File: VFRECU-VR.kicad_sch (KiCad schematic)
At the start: 39 parts, among them J1 USB_B_Mini, J1 USB_C_Receptacle_USB2.0, J17 Conn_01x06, J4 1-776087-1, J7 MUSBD111M0, M1 Module-power_12and5V-0.2, M3 Module-knock-0.2, M5 Module-wbo-0.5, M6 Module:mega-mcu100/0.2, M7 Module-wbo-0.5, P1 Pad, P2 Pad, P3 Pad, P4 Pad, U4 JDY-33

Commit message: Don't need proofreading I'm a FREAK
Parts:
- removed R17: 56k, hellen-one-common:R0603, symbol hellen-one-common:Res
- removed R19: 12k, hellen-one-common:R0603, symbol hellen-one-common:Res
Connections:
- net IN_BUTTON2 renamed Clutch/kickstandswitch
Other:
- note removed: "Cam/Crank- offset"

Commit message: More routing changes
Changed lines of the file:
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@@
 	)
 	(junction
-		(at 312.42 33.02)
-		(diameter 0)
-		(color 0 0 0 0)
-	)
-	(junction
 		(at 346.71 166.37)
 		(diameter 0)
@@
 	)
 	(junction
+		(at 312.42 26.67)
+		(diameter 0)
+		(color 0 0 0 0)
+	)
+	(junction
 		(at 168.91 148.59)
 		(diameter 0)
@@
 	(bus
 		(pts
-			(xy 138.43 25.4) (xy 342.9 25.4)
+			(xy 138.43 26.67) (xy 312.42 26.67)
 		)
 		(stroke
@@
 	(bus
 		(pts
-			(xy 311.15 -27.94) (xy 311.15 33.02)
+			(xy 312.42 -27.94) (xy 312.42 26.67)
 		)
 		(stroke
@@
 		)
 	)
-	(bus
-		(pts
-			(xy 342.9 33.02) (xy 312.42 33.02)
-		)
-		(stroke
-			(width 0)
-			(type default)
-		)
-	)
 	(wire
 		(pts
@@
 	(bus
 		(pts
-			(xy 342.9 25.4) (xy 342.9 33.02)
+			(xy 312.42 26.67) (xy 312.42 54.61)
 		)
 		(stroke
@@
 	(bus
 		(pts
-			(xy 138.43 34.29) (xy 138.43 25.4)
+			(xy 138.43 34.29) (xy 138.43 26.67)
 		)
 		(stroke
@@
 		)
 	)
-	(bus
-		(pts
-			(xy 312.42 33.02) (xy 312.42 54.61)
-		)
-		(stroke
-			(width 0)
-			(type default)
-		)
-	)
 	(wire
 		(pts
@@
 	(bus
 		(pts
-			(xy 270.51 -27.94) (xy 311.15 -27.94)
+			(xy 270.51 -27.94) (xy 312.42 -27.94)
 		)
 		(stroke
@@
 		)
 		(stroke
-			(width 0)
-			(type default)
-		)
-	)
-	(bus
-		(pts
-			(xy 311.15 33.02) (xy 312.42 33.02)
-		)
-		(stroke

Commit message: Moved Ground Planes to Internal Layers
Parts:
- removed H2: MountingHole_Pad, MountingHole:MountingHole_3.2mm_M3_DIN965_Pad, symbol Mechanical:MountingHole_Pad
- removed J1: USB_C_Receptacle_USB2.0, Connector_USB:USB_C_Receptacle_XKB_U262-16XN-4BVC11, symbol Connector:USB_C_Receptacle_USB2.0
- removed J17 (x2): Conn_01x06, Connector_PinHeader_2.54mm:PinHeader_1x06_P2.54mm_Vertical, symbol Connector_Generic:Conn_01x06
- removed J7: MUSBD111M0, usbb:CONN4_BD111M0_AMP, symbol usbb:MUSBD111M0
- removed P1, P2, P3, P4: Pad, hellen-one-common:PAD-TH, symbol hellen-one-common:Pad
- removed R3, R6: 5.6k, hellen-one-common:R0603, symbol hellen-one-common:Res
- removed R30: 0, hellen-one-common:R0603, symbol hellen-one-common:Res
- removed R4: Jumper-Pad-Pad, hellen-one-common:PAD-0805-PAD, symbol hellen-one-common:Jumper-Pad-Pad
- added R4: 0, Resistor_SMD:R_0402_1005Metric, symbol Device:R
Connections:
- net INTAKEFLAP: now also J4.4; no longer J4.5
- net IN_AUX1: now also J4.12; no longer J4.13
- net IN_AUX2: now also J4.13; no longer J4.11
- net IN_FLEX: now also J4.11; no longer J4.12
- net OUT_LS2: now also J4.5; no longer J4.6
- net OUT_LS3: now also J4.6; no longer J4.4
- net PG_5VP: now also M6.N12 (SPI3_MOSI_(PC12)), R4.2
- net at M1.E6 (PG_5VP): now also R4.1
- net DC1_DIR: no longer names the net of M6.E21 (OUT_PWM4_(PC8))
- net DC1_PWM: no longer names the net of M6.E20 (OUT_PWM3_(PC7))
- net DC2_PWM: no longer names the net of M6.E22 (OUT_PWM5_(PC9))
- net VR1_THRESHOLD: no longer names the net of M6.E23 (OUT_PWM6_(PD14))
- no-connect marks 35 -> 31
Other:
- note removed: "A"

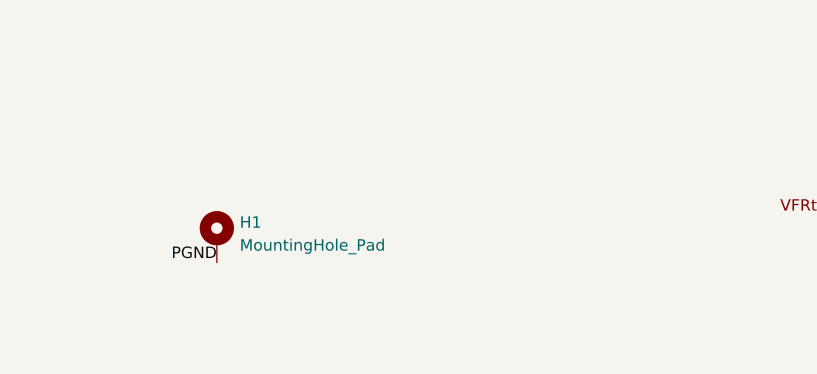
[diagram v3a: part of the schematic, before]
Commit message: Fixed pads
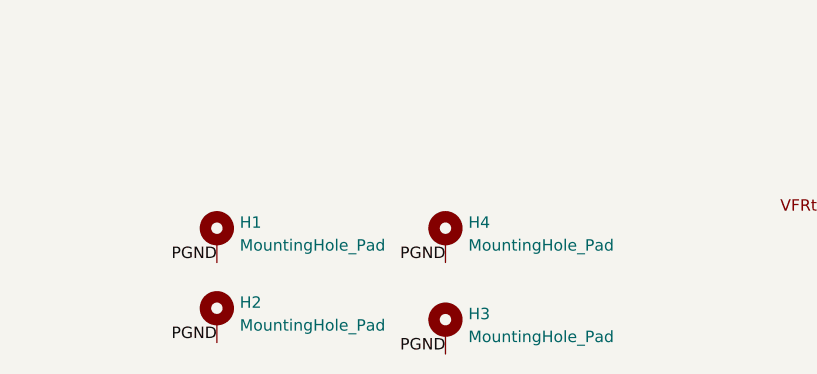
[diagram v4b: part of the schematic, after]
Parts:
- added H2, H3, H4: MountingHole_Pad, MountingHole:MountingHole_3.2mm_M3_DIN965_Pad, symbol Mechanical:MountingHole_Pad
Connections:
- net GND: now also H2.1, H3.1, H4.1
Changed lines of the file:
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@@
 		)
 	)
+	(label "PGND"
+		(at 228.6 401.32 180)
+		(fields_autoplaced yes)
+		(effects
+			(font
+				(size 1.27 1.27)
+			)
+			(justify right bottom)
+		)
+	)
 	(label "INJ3"
 		(at 247.65 138.43 0)
@@
 		)
 	)
+	(label "PGND"
+		(at 203.2 400.05 180)
+		(fields_autoplaced yes)
+		(effects
+			(font
+				(size 1.27 1.27)
+			)
+			(justify right bottom)
+		)
+	)
 	(label "VR1-"
 		(at 133.35 229.87 0)
@@
 		)
 	)
+	(label "PGND"
+		(at 228.6 391.16 180)
+		(fields_autoplaced yes)
+		(effects
+			(font
+				(size 1.27 1.27)
+			)
+			(justify right bottom)
+		)
+	)
 	(label "12VSWITCHED"
 		(at 138.43 148.59 90)
@@
 	(symbol
 		(lib_id "Mechanical:MountingHole_Pad")
+		(at 203.2 397.51 0)
+		(unit 1)
+		(exclude_from_sim no)
+		(in_bom yes)
+		(on_board yes)
+		(dnp no)
+		(fields_autoplaced yes)
+		(property "Reference" "H2"
+			(at 205.74 395.605 0)
+			(effects
+				(font
+					(size 1.27 1.27)
+				)
+				(justify left)
+			)
+		)
+		(property "Value" "MountingHole_Pad"
+			(at 205.74 398.145 0)
+			(effects
+				(font
+					(size 1.27 1.27)
+				)
+				(justify left)
+			)
+		)
+		(property "Footprint" "MountingHole:MountingHole_3.2mm_M3_DIN965_Pad"
+			(at 203.2 397.51 0)
+			(effects
+				(font
+					(size 1.27 1.27)
+				)
+				(hide yes)
+			)
+		)
+		(property "Datasheet" "~"
+			(at 203.2 397.51 0)
+			(effects
+				(font
+					(size 1.27 1.27)
+				)
+				(hide yes)
+			)
+		)
+		(property "Description" ""
+			(at 203.2 397.51 0)
+			(effects
+				(font
+					(size 1.27 1.27)
+				)
+				(hide yes)
+			)
+		)
+		(pin "1"
+		)
+		(instances
+			(project "VFRECU-VR"
+				(path "/90b72e19-92bc-40db-bd4d-f17fb5de93ea"
+					(reference "H2")
+					(unit 1)
+				)
+			)
+		)
+	)
+	(symbol
+		(lib_id "Mechanical:MountingHole_Pad")
 		(at 203.2 388.62 0)
 		(unit 1)
@@
 	)
 	(symbol
+		(lib_id "Mechanical:MountingHole_Pad")
+		(at 228.6 398.78 0)
+		(unit 1)
+		(exclude_from_sim no)
+		(in_bom yes)
+		(on_board yes)
+		(dnp no)
+		(fields_autoplaced yes)
+		(property "Reference" "H3"
+			(at 231.14 396.875 0)
+			(effects
+				(font
+					(size 1.27 1.27)
+				)
+				(justify left)
+			)
+		)
+		(property "Value" "MountingHole_Pad"
+			(at 231.14 399.415 0)
+			(effects
+				(font
+					(size 1.27 1.27)
+				)
+				(justify left)
+			)
+		)
+		(property "Footprint" "MountingHole:MountingHole_3.2mm_M3_DIN965_Pad"
+			(at 228.6 398.78 0)
+			(effects
+				(font
+					(size 1.27 1.27)
+				)
+				(hide yes)
+			)
+		)
+		(property "Datasheet" "~"
+			(at 228.6 398.78 0)
+			(effects
+				(font
+					(size 1.27 1.27)
+				)
+				(hide yes)
+			)
+		)
+		(property "Description" ""
+			(at 228.6 398.78 0)
+			(effects
+				(font
+					(size 1.27 1.27)
+				)
+				(hide yes)
+			)
+		)
+		(pin "1"
+		)
+		(instances
+			(project "VFRECU-VR"
+				(path "/90b72e19-92bc-40db-bd4d-f17fb5de93ea"
+					(reference "H3")
+					(unit 1)
+				)
+			)
+		)
+	)
+	(symbol
 		(lib_id "power:+5VA")
 		(at 152.4 30.48 0)
@@
 					(unit 1)
 				)
+			)
+		)
+	)
+	(symbol
+		(lib_id "Mechanical:MountingHole_Pad")
+		(at 228.6 388.62 0)
+		(unit 1)
+		(exclude_from_sim no)
+		(in_bom yes)
+		(on_board yes)
+		(dnp no)
+		(fields_autoplaced yes)
+		(property "Reference" "H4"
+			(at 231.14 386.715 0)
+			(effects
+				(font
+					(size 1.27 1.27)
+				)
+				(justify left)
+			)
+		)
+		(property "Value" "MountingHole_Pad"
+			(at 231.14 389.255 0)
+			(effects
+				(font
+					(size 1.27 1.27)
+				)
+				(justify left)
+			)
+		)
+		(property "Footprint" "MountingHole:MountingHole_3.2mm_M3_DIN965_Pad"
+			(at 228.6 388.62 0)
+			(effects
+				(font
+					(size 1.27 1.27)
+				)
+				(hide yes)
+			)
+		)
+		(property "Datasheet" "~"
+			(at 228.6 388.62 0)
+			(effects
+				(font
+					(size 1.27 1.27)
+				)
+				(hide yes)
+			)
+		)
+		(property "Description" ""
+			(at 228.6 388.62 0)
+			(effects
+				(font
+					(size 1.27 1.27)
+				)
+				(hide yes)
+			)
+		)
+		(pin "1"
+		)
+		(instances
+			(project "VFRECU-VR"
+				(path "/90b72e19-92bc-40db-bd4d-f17fb5de93ea"
+					(reference "H4")
+					(unit 1)
+				)

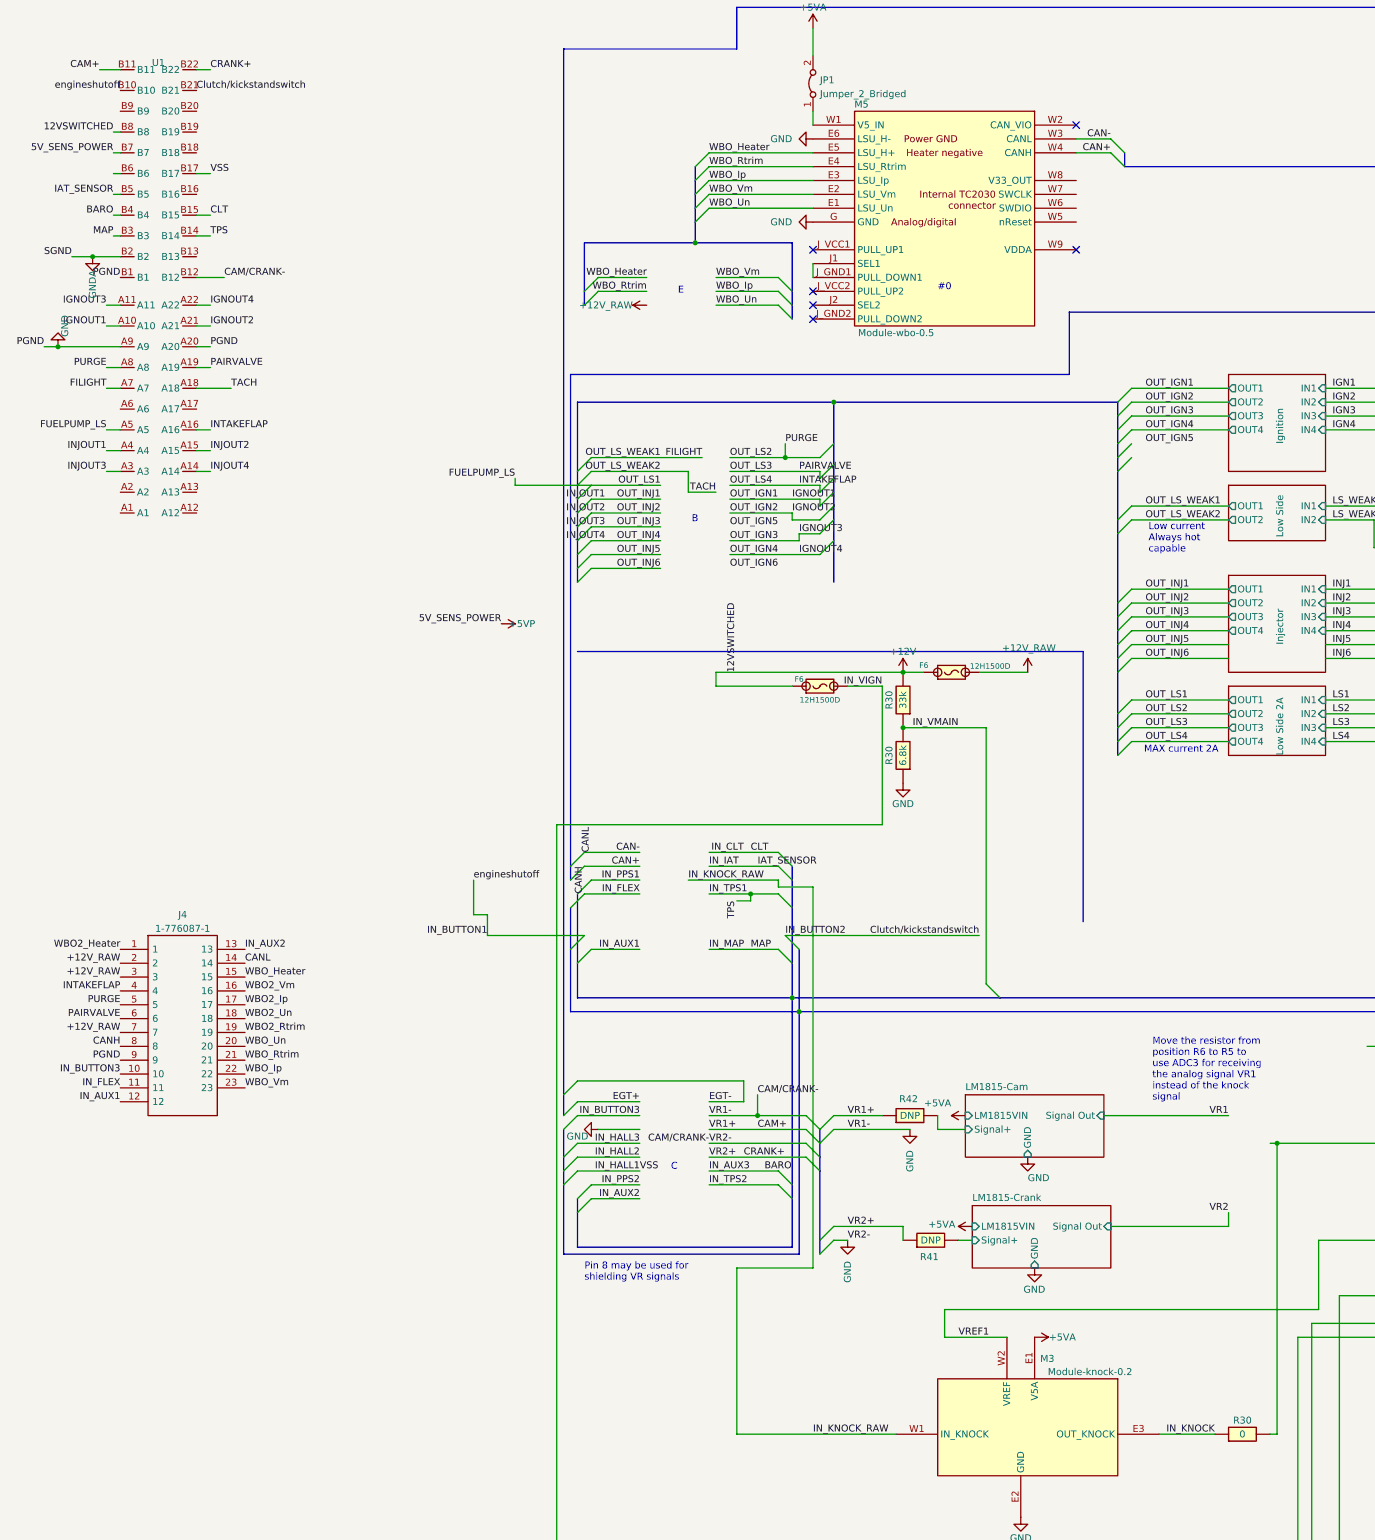
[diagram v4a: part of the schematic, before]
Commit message: Added knock detection hardware
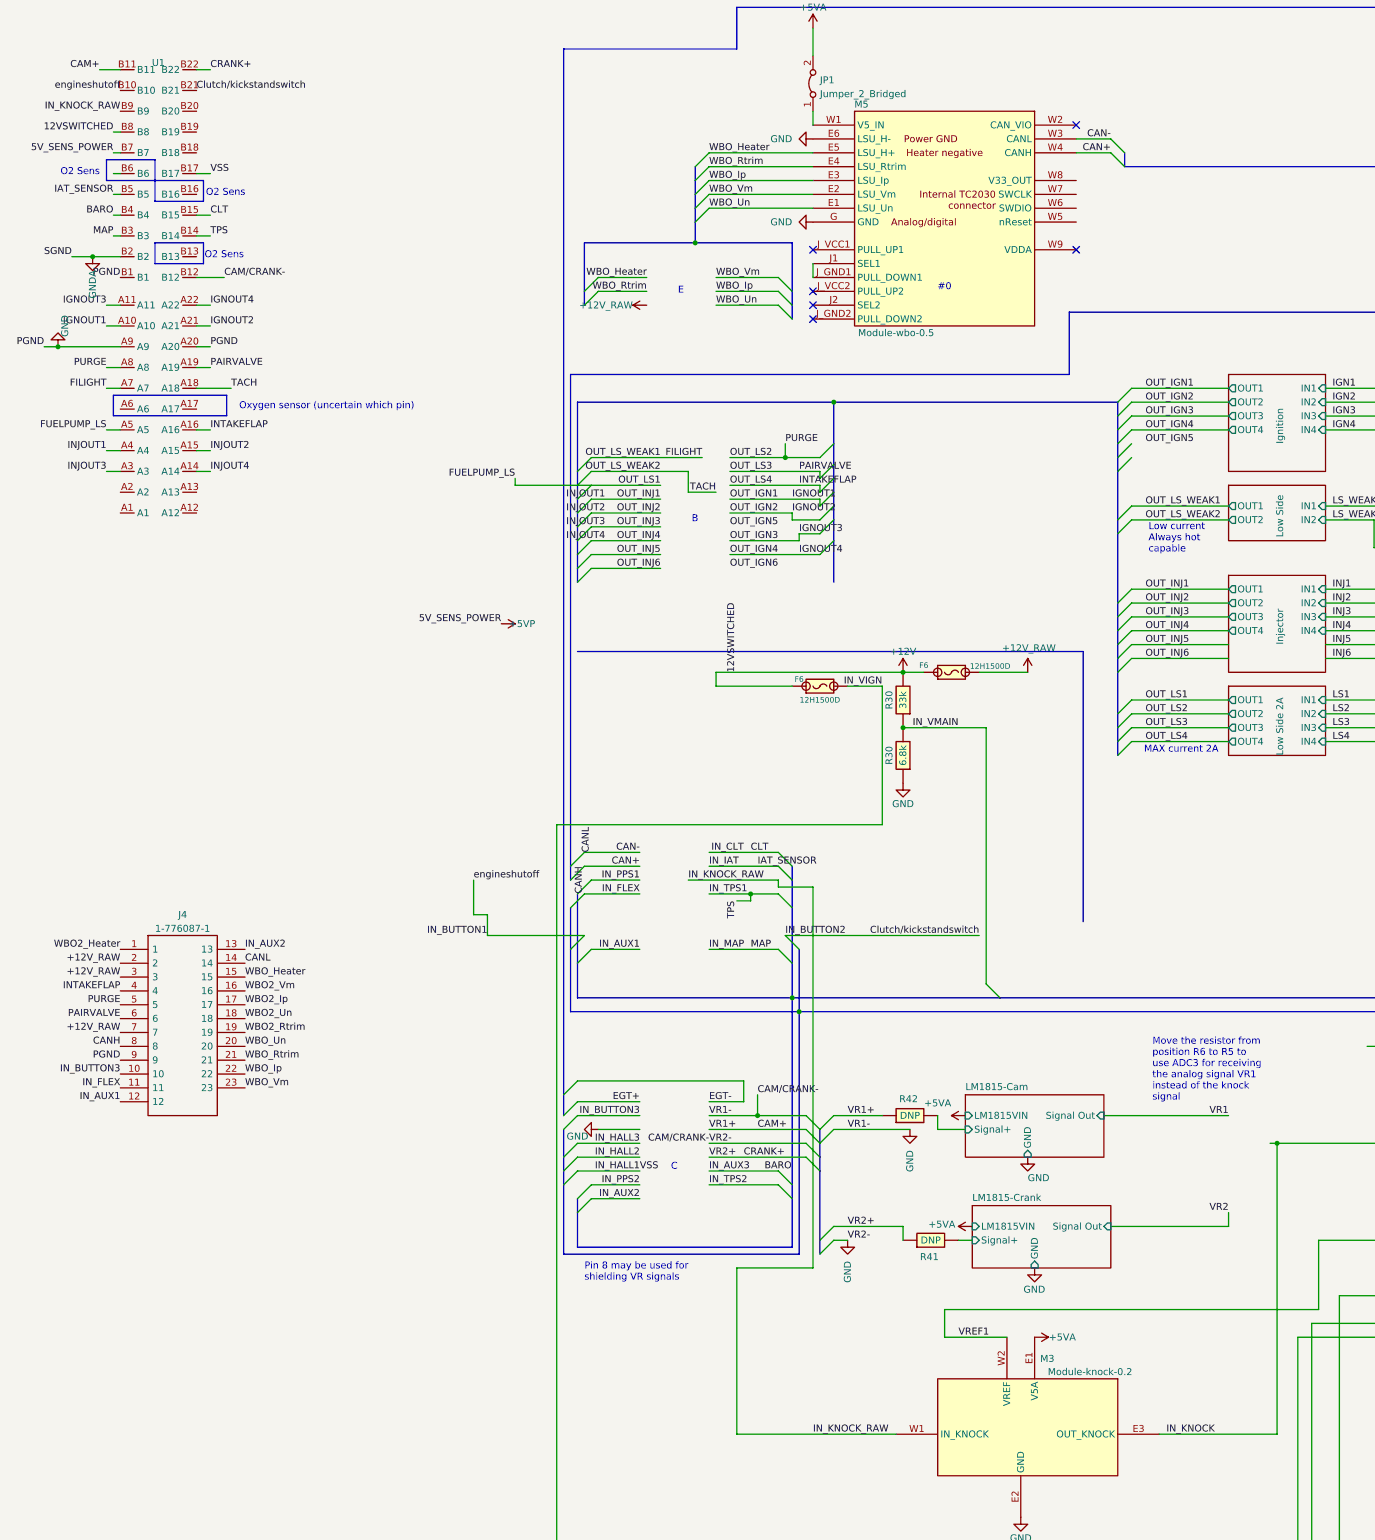
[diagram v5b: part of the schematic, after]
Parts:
- removed R30: 0, hellen-one-common:R0603, symbol hellen-one-common:Res
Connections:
- net IN_KNOCK is gone; now on net ADC3: M3.E3 (OUT_KNOCK)
- net IN_KNOCK_RAW: now also U1.B9
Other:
- note added: "O2 Sens"
- note added: "Oxygen sensor (uncertain which pin)"
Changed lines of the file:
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@@
 	(wire
 		(pts
-			(xy 226.06 288.29) (xy 215.9 288.29)
+			(xy 215.9 288.29) (xy 237.49 288.29)
 		)
 		(stroke
@@
 	(wire
 		(pts
-			(xy 236.22 288.29) (xy 237.49 288.29)
-		)
-		(stroke
-			(width 0)
-			(type default)
-		)
-	)
-	(wire
-		(pts
 			(xy 24.13 49.53) (xy 25.4 49.53)
 		)
@@
 		)
 	)
+	(rectangle
+		(start 31.75 58.42)
+		(end 40.64 62.23)
+		(stroke
+			(width 0)
+			(type default)
+		)
+		(fill
+			(type none)
+		)
+	)
+	(rectangle
+		(start 22.86 54.61)
+		(end 31.75 58.42)
+		(stroke
+			(width 0)
+			(type default)
+		)
+		(fill
+			(type none)
+		)
+	)
+	(rectangle
+		(start 31.75 69.85)
+		(end 40.64 73.66)
+		(stroke
+			(width 0)
+			(type default)
+		)
+		(fill
+			(type none)
+		)
+	)
+	(rectangle
+		(start 24.13 97.79)
+		(end 44.8976 101.5527)
+		(stroke
+			(width 0)
+			(type default)
+		)
+		(fill
+			(type none)
+		)
+	)
 	(text "Bluetooth Module"
 		(exclude_from_sim no)
@@
 		)
 	)
+	(text "O2 Sens\n"
+		(exclude_from_sim no)
+		(at 18.034 56.896 0)
+		(effects
+			(font
+				(size 1.27 1.27)
+			)
+		)
+	)
 	(text "General purpose bus"
 		(exclude_from_sim no)
@@
 		)
 	)
+	(text "O2 Sens\n"
+		(exclude_from_sim no)
+		(at 44.45 72.136 0)
+		(effects
+			(font
+				(size 1.27 1.27)
+			)
+		)
+	)
 	(text "Move the resistor from\nposition R143 to R145 to\nenable the CAN WAKEUP\nfunction. The AUX1 analog\ninput will be unavailable."
 		(exclude_from_sim no)
@@
 		)
 	)
+	(text "O2 Sens\n"
+		(exclude_from_sim no)
+		(at 44.704 60.706 0)
+		(effects
+			(font
+				(size 1.27 1.27)
+			)
+		)
+	)
 	(text "Move the resistor from\nposition R6 to R5 to\nuse ADC3 for receiving\nthe analog signal VR1\ninstead of the knock\nsignal"
 		(exclude_from_sim no)
@@
 		)
 	)
+	(text "Oxygen sensor (uncertain which pin)"
+		(exclude_from_sim no)
+		(at 63.246 99.822 0)
+		(effects
+			(font
+				(size 1.27 1.27)
+			)
+		)
+	)
 	(text "Ignition"
 		(exclude_from_sim no)
@@
 		)
 	)
+	(label "IN_KNOCK_RAW"
+		(at 25.4 45.72 180)
+		(fields_autoplaced yes)
+		(effects
+			(font
+				(size 1.27 1.27)
+			)
+			(justify right bottom)
+		)
+	)
 	(label "IN_HALL1"
 		(at 273.05 240.03 180)
@@
 					(unit 1)
 				)
-			)
-		)
-	)
-	(symbol
-		(lib_id "hellen-one-common:Res")
-		(at 226.06 288.29 0)
-		(unit 1)
-		(exclude_from_sim no)
-		(in_bom yes)
-		(on_board yes)
-		(dnp no)
-		(property "Reference" "R30"
-			(at 231.14 285.75 0)
-			(effects
-				(font
-					(size 1.27 1.27)
-				)
-			)
-		)
-		(property "Value" "0"
-			(at 231.14 288.29 0)
-			(effects
-				(font
-					(size 1.27 1.27)
-				)
-			)
-		)
-		(property "Footprint" "hellen-one-common:R0603"
-			(at 229.87 292.1 0)
-			(effects
-				(font
-					(size 1.27 1.27)
-				)
-				(hide yes)
-			)
-		)
-		(property "Datasheet" ""
-			(at 226.06 288.29 0)
-			(effects
-				(font
-					(size 1.27 1.27)
-				)
-				(hide yes)
-			)
-		)
-		(property "Description" ""
-			(at 226.06 288.29 0)
-			(effects
-				(font
-					(size 1.27 1.27)
-				)
-				(hide yes)
-			)
-		)
-		(property "LCSC" "C21189"
-			(at 226.06 288.29 0)
-			(effects
-				(font
-					(size 1.27 1.27)
-				)
-				(hide yes)
-			)
-		)
-		(pin "1"
-		)
-		(pin "2"
-		)
-		(instances
-			(project "alphax_8ch"
-				(path "/63d2dd9f-d5ff-4811-a88d-0ba932475460"
-					(reference "R30")
-					(unit 1)
-				)
-				(path "/63d2dd9f-d5ff-4811-a88d-0ba932475460/9f286606-17ad-4292-b95a-d7d4de96430a"
-					(reference "R67")
-					(unit 1)
-				)
-			)
-			(project "uaeficopiedtovfr"
-				(path "/90b72e19-92bc-40db-bd4d-f17fb5de93ea"
-					(reference "R6")
-					(unit 1)
-				)
-			)
-			(project "uaefi"
-				(path "/ac264c30-3e9a-4be2-b97a-9949b68bd497"
-					(reference "R6")
-					(unit 1)
-				)
